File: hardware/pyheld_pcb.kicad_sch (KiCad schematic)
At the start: 0 parts

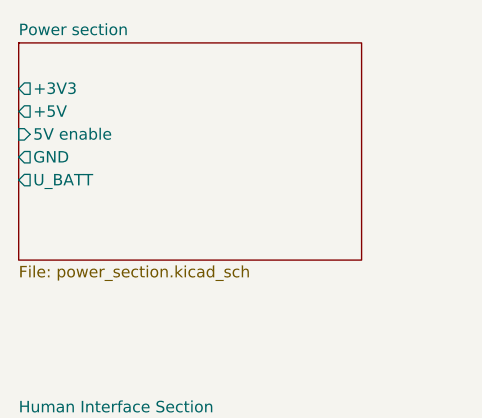
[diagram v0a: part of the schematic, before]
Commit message: Human Interface section finished
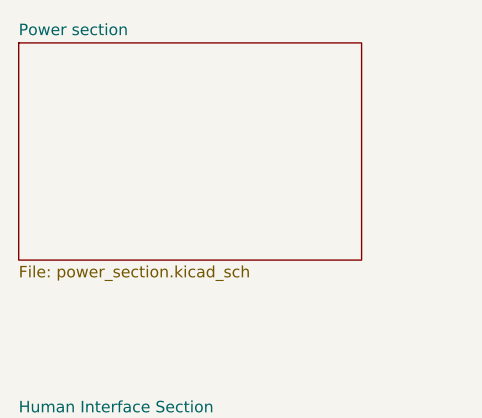
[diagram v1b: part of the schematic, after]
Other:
- sheet Power section ports: added none; removed +3V3, +5V, 5V enable, GND, U_BATT
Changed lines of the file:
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@@
-			)
-		)
-		(pin "+3V3" output
-			(at 49.53 45.72 180)
-			(effects
-				(font
-					(size 1.27 1.27)
-				)
-				(justify left)
-			)
-		)
-		(pin "+5V" output
-			(at 49.53 48.26 180)
-			(effects
-				(font
-					(size 1.27 1.27)
-				)
-				(justify left)
-			)
-		)
-		(pin "5V enable" input
-			(at 49.53 50.8 180)
-			(effects
-				(font
-					(size 1.27 1.27)
-				)
-				(justify left)
-			)
-		)
-		(pin "GND" output
-			(at 49.53 53.34 180)
-			(effects
-				(font
-					(size 1.27 1.27)
-				)
-				(justify left)
-			)
-		)
-		(pin "U_BATT" output
-			(at 49.53 55.88 180)
-			(effects
-				(font
-					(size 1.27 1.27)
-				)
-				(justify left)
 			)
 		)

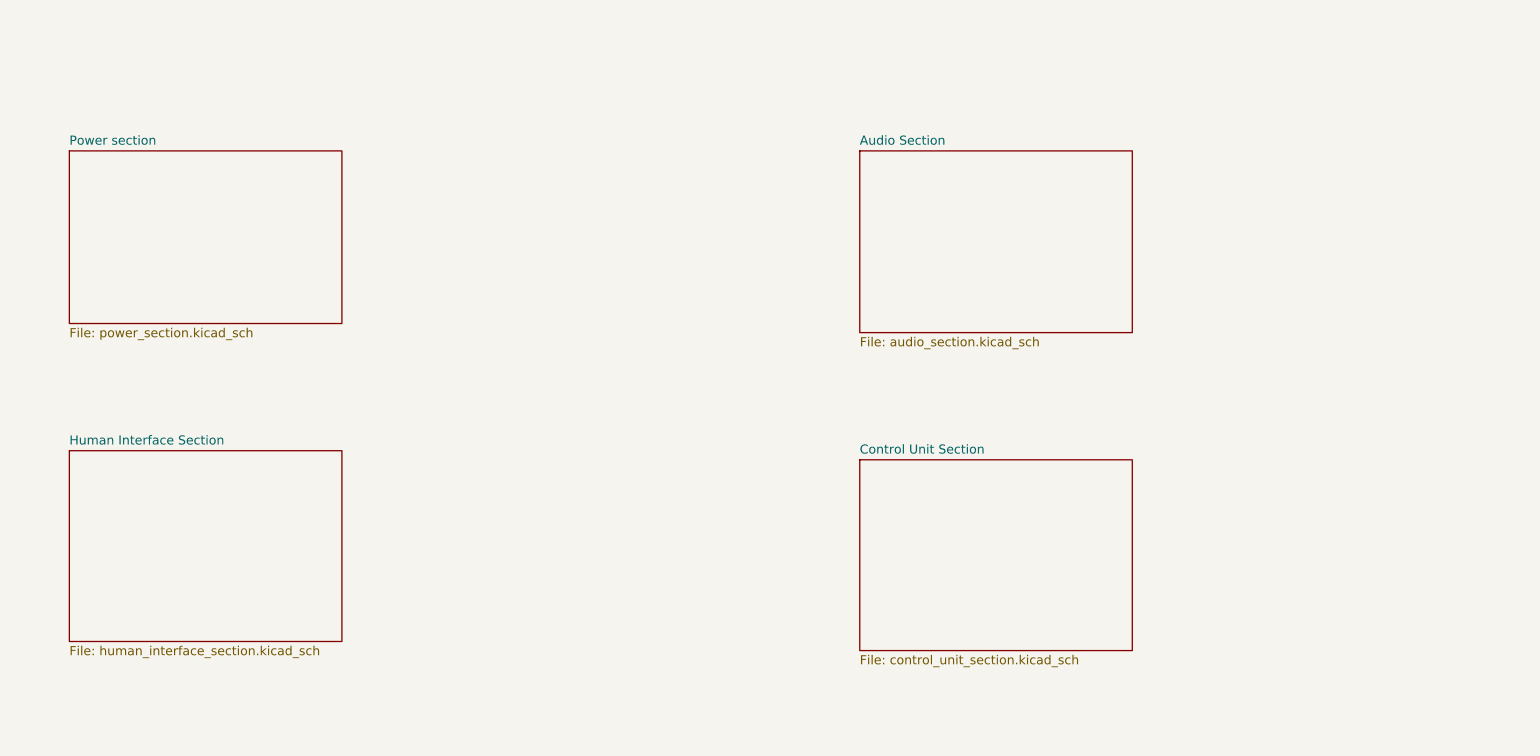
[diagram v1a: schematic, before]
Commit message: Moved MCU to general section
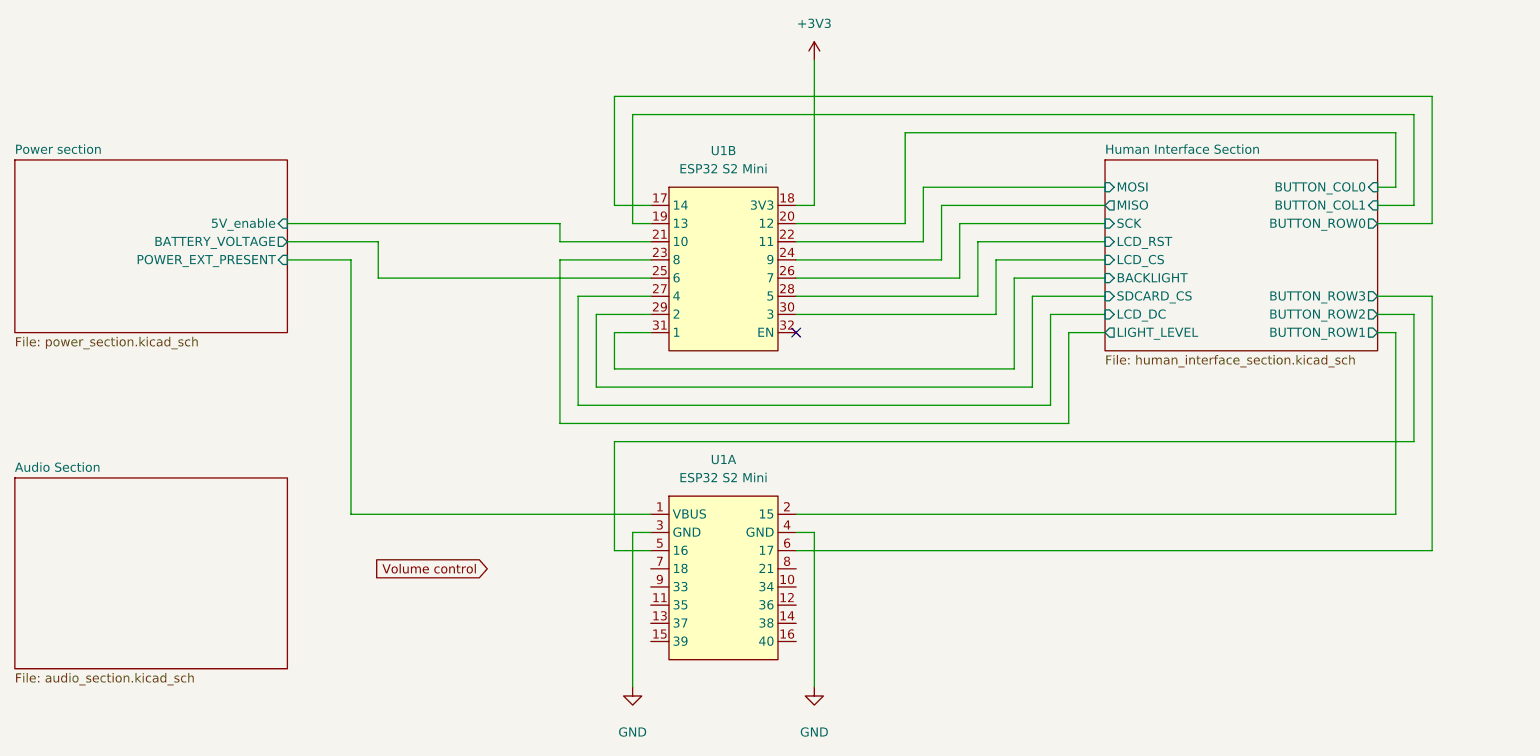
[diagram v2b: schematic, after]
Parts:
- added U1: ESP32 S2 Mini, additional_footprints:ESP32 S2 Mini Headers, symbol additional_symbols:ESP32_S2_Mini
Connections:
- new net +3V3: U1.18 (3V3)
- new net GND: U1.3 (GND), U1.4 (GND)
- new net Human Interface Section/BACKLIGHT: U1.31 (1)
- new net Human Interface Section/BUTTON_COL0: U1.20 (12)
- new net Human Interface Section/BUTTON_COL1: U1.19 (13)
- new net Human Interface Section/BUTTON_ROW0: U1.17 (14)
- new net Human Interface Section/BUTTON_ROW1: U1.2 (15)
- new net Human Interface Section/BUTTON_ROW2: U1.5 (16)
- new net Human Interface Section/BUTTON_ROW3: U1.6 (17)
- new net Human Interface Section/LCD_CS: U1.30 (3)
- new net Human Interface Section/LCD_DC: U1.27 (4)
- new net Human Interface Section/LCD_RST: U1.28 (5)
- new net Human Interface Section/LIGHT_LEVEL: U1.23 (8)
- new net Human Interface Section/MISO: U1.24 (9)
- new net Human Interface Section/MOSI: U1.22 (11)
- new net Human Interface Section/SCK: U1.26 (7)
- new net Human Interface Section/SDCARD_CS: U1.29 (2)
- new net Power section/5V_enable: U1.21 (10)
- new net Power section/BATTERY_VOLTAGE: U1.25 (6)
- new net Power section/POWER_EXT_PRESENT: U1.1 (VBUS)
- no-connect marks 0 -> 1
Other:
- removed sheet Control Unit Section
- sheet Human Interface Section ports: added BACKLIGHT, BUTTON_COL0, BUTTON_COL1, BUTTON_ROW0, BUTTON_ROW1, BUTTON_ROW2, BUTTON_ROW3, LCD_CS, LCD_DC, LCD_RST, LIGHT_LEVEL, MISO, MOSI, SCK, SDCARD_CS; removed none
- sheet Power section ports: added 5V_enable, BATTERY_VOLTAGE, POWER_EXT_PRESENT; removed none

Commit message: Removed additional audio circuits Simplified connections -> change DAC (WAU8812 will be difficult by now to make working)
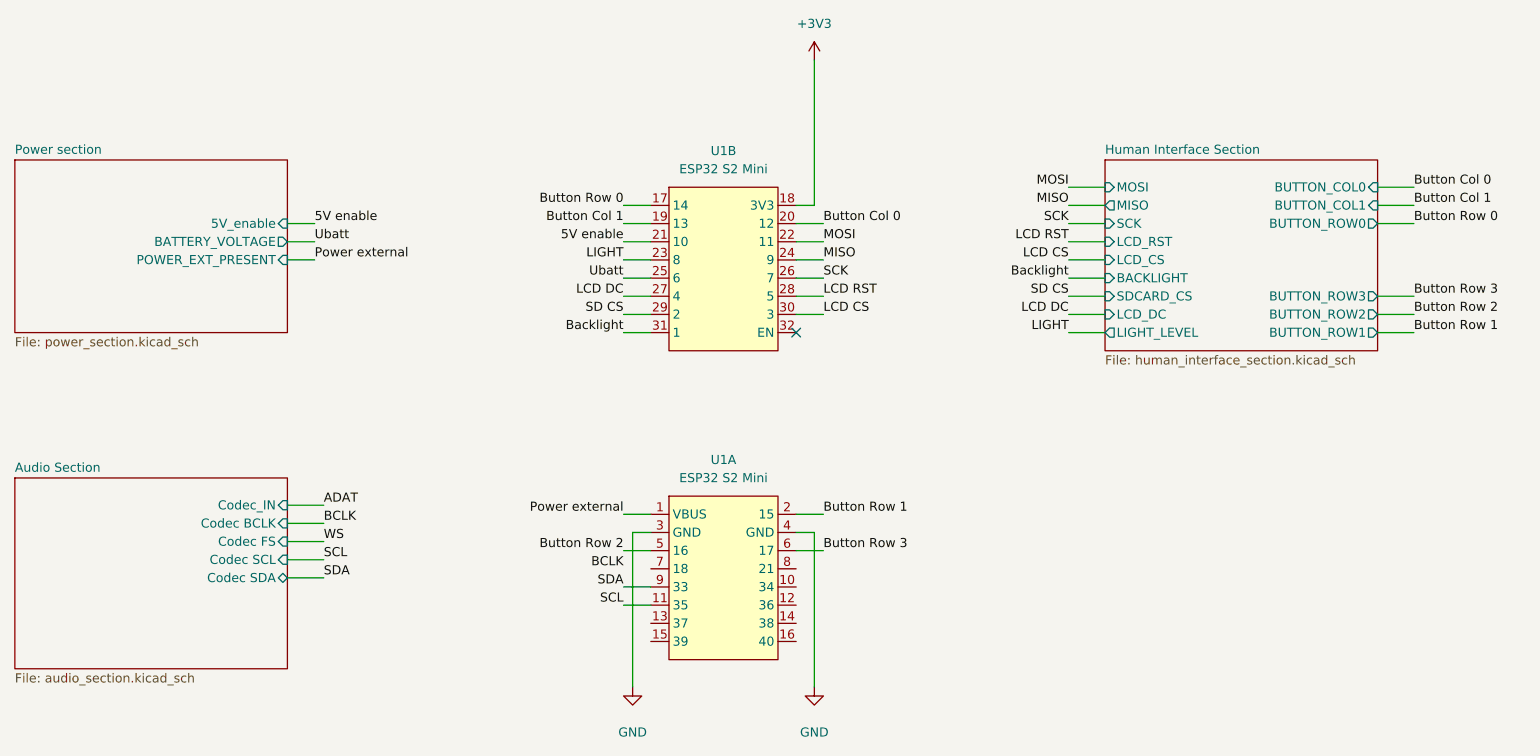
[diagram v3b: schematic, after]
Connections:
- net SCL: now reaches U1.11 (35)
- net SDA: now reaches U1.9 (33)
- net Human Interface Section/BACKLIGHT renamed Backlight
- net Human Interface Section/BUTTON_COL0 renamed Button Col 0
- net Human Interface Section/BUTTON_COL1 renamed Button Col 1
- net Human Interface Section/BUTTON_ROW0 renamed Button Row 0
- net Human Interface Section/BUTTON_ROW1 renamed Button Row 1
- net Human Interface Section/BUTTON_ROW2 renamed Button Row 2
- net Human Interface Section/BUTTON_ROW3 renamed Button Row 3
- net Human Interface Section/LCD_CS renamed LCD CS
- net Human Interface Section/LCD_DC renamed LCD DC
- net Human Interface Section/LCD_RST renamed LCD RST
- net Human Interface Section/LIGHT_LEVEL renamed LIGHT
- net Human Interface Section/MISO renamed MISO
- net Human Interface Section/MOSI renamed MOSI
- net Human Interface Section/SCK renamed SCK
- net Human Interface Section/SDCARD_CS renamed SD CS
- net Power section/5V_enable renamed 5V enable
- net Power section/BATTERY_VOLTAGE renamed Ubatt
- net Power section/POWER_EXT_PRESENT renamed Power external
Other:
- sheet Audio Section ports: added Codec BCLK, Codec FS, Codec SCL, Codec SDA, Codec_IN; removed none
